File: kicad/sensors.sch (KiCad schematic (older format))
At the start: 4 parts

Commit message: snapshot
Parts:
- added I1, I2: INA381, HH_TexasInstruments:INA381-WSON, symbol HH_TexasInstruments:INA381
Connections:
- net GND: now also I1.4 (RESET), I1.PAD (GND), I2.4 (RESET), I2.PAD (GND)
- new net 3V3: I1.2 (VS+), I1.5 (CMPREF), I2.2 (VS+), I2.5 (CMPREF)
- new net OUT3: I1.6 (CMPIN), I1.7 (VOUT)
- new net OUT4: I2.6 (CMPIN), I2.7 (VOUT)
- new net S3+: I1.1 (IN+)
- new net S3-: I1.8 (IN-)
- new net S4+: I2.1 (IN+)
- new net S4-: I2.8 (IN-)
- no-connect marks 0 -> 2
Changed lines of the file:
@@
 Wire Wire Line
 	7150 4350 7150 4550
+$Comp
+L HH_TexasInstruments:INA381 I1
+U 1 1 5FC9F5FA
+P 5700 5400
+F 0 "I1" H 5700 5915 50  0000 C CNN
+F 1 "INA381" H 5700 5824 50  0000 C CNN
+F 2 "HH_TexasInstruments:INA381-WSON" H 5700 5400 50  0001 C CNN
+F 3 "https://www.ti.com/lit/ds/symlink/ina381.pdf" H 5700 5400 50  0001 C CNN
+F 4 "296-50475-1-ND" H 5700 5400 50  0001 C CNN "Digi-Key Part Number"
+F 5 "Texas Instruments" H 5700 5400 50  0001 C CNN "Manufacturer"
+F 6 "INA381A1IDSGR" H 5700 5400 50  0001 C CNN "Manufacturer Part Number"
+F 7 "LOW COST CURRENT SENSOR WITH COM" H 5700 5400 50  0001 C CNN "Description"
+	1    5700 5400
+	1    0    0    -1
+$EndComp
+$Comp
+L HH_TexasInstruments:INA381 I2
+U 1 1 5FC9FD95
+P 5700 6500
+F 0 "I2" H 5700 7015 50  0000 C CNN
+F 1 "INA381" H 5700 6924 50  0000 C CNN
+F 2 "HH_TexasInstruments:INA381-WSON" H 5700 6500 50  0001 C CNN
+F 3 "https://www.ti.com/lit/ds/symlink/ina381.pdf" H 5700 6500 50  0001 C CNN
+F 4 "296-50475-1-ND" H 5700 6500 50  0001 C CNN "Digi-Key Part Number"
+F 5 "Texas Instruments" H 5700 6500 50  0001 C CNN "Manufacturer"
+F 6 "INA381A1IDSGR" H 5700 6500 50  0001 C CNN "Manufacturer Part Number"
+F 7 "LOW COST CURRENT SENSOR WITH COM" H 5700 6500 50  0001 C CNN "Description"
+	1    5700 6500
+	1    0    0    -1
+$EndComp
+NoConn ~ 5100 5550
+NoConn ~ 5100 6650
+Text HLabel 7200 5950 2    50   Input ~ 0
+GND
+Wire Wire Line
+	6300 5250 6500 5250
+Wire Wire Line
+	7050 5250 7050 5950
+Wire Wire Line
+	7050 5950 7200 5950
+Wire Wire Line
+	7050 5950 7050 6350
+Wire Wire Line
+	7050 6350 6500 6350
+Connection ~ 7050 5950
+Wire Wire Line
+	6500 6350 6500 6450
+Wire Wire Line
+	6500 6450 6300 6450
+Connection ~ 6500 6350
+Wire Wire Line
+	6500 6350 6300 6350
+Wire Wire Line
+	6500 5250 6500 5350
+Wire Wire Line
+	6500 5350 6300 5350
+Connection ~ 6500 5250
+Wire Wire Line
+	6500 5250 7050 5250
+Text HLabel 7150 5150 2    50   Input ~ 0
+3V3
+Wire Wire Line
+	7150 5150 6700 5150
+Wire Wire Line
+	6700 5150 6700 6250
+Wire Wire Line
+	6700 6250 6300 6250
+Connection ~ 6700 5150
+Wire Wire Line
+	6700 5150 6300 5150
+Text HLabel 5100 5150 0    50   Input ~ 0
+S3+
+Text HLabel 5100 5250 0    50   Input ~ 0
+S3-
+Text HLabel 5100 6250 0    50   Input ~ 0
+S4+
+Text HLabel 5100 6350 0    50   Input ~ 0
+S4-
+Text HLabel 4600 5350 0    50   Input ~ 0
+OUT3
+Text HLabel 4600 6450 0    50   Input ~ 0
+OUT4
+Text HLabel 5100 5650 0    50   Input ~ 0
+3V3
+Text HLabel 5100 6750 0    50   Input ~ 0
+3V3
+Wire Wire Line
+	5100 5350 4800 5350
+Wire Wire Line
+	4800 5350 4800 5750
+Wire Wire Line
+	4800 5750 5100 5750
+Connection ~ 4800 5350
+Wire Wire Line
+	4800 5350 4600 5350
+Wire Wire Line
+	5100 6450 4800 6450
+Wire Wire Line
+	4800 6450 4800 6850
+Wire Wire Line
+	4800 6850 5100 6850
+Connection ~ 4800 6450
+Wire Wire Line
+	4800 6450 4600 6450
 $EndSCHEMATC

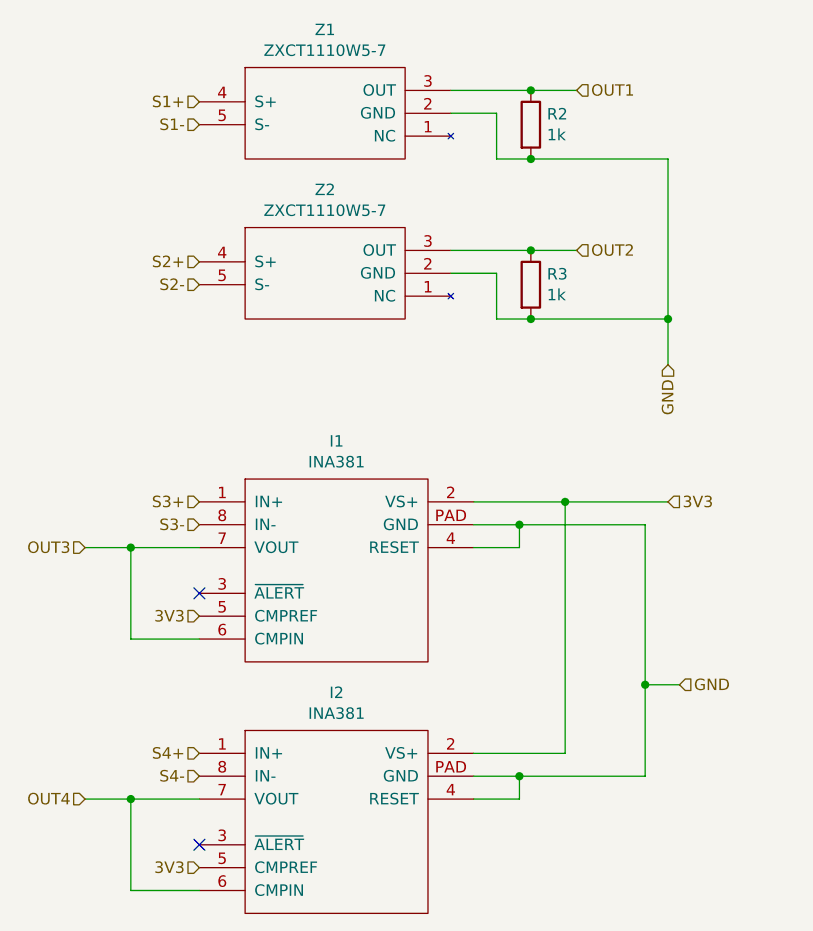
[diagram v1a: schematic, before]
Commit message: switch clock and add bypass
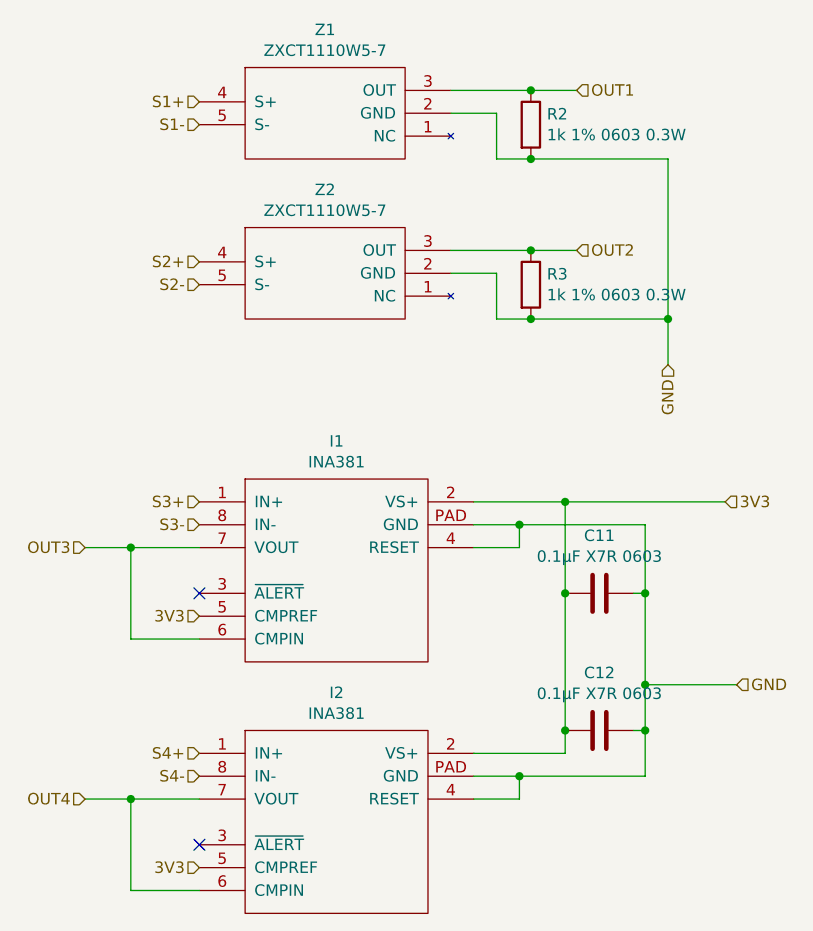
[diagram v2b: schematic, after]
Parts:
- added C11, C12: 0.1µF X7R 0603, Capacitor_SMD:C_0603_1608Metric, symbol Device:C
- R2, R3: value 1k -> 1k 1% 0603 0.3W
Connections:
- net 3V3: now also C11.2, C12.2
- net GND: now also C11.1, C12.1
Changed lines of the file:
@@
 P 6550 3500
 F 0 "R2" H 6620 3546 50  0000 L CNN
-F 1 "1k" H 6620 3455 50  0000 L CNN
+F 1 "1k 1% 0603 0.3W" H 6620 3455 50  0000 L CNN
 F 2 "Resistor_SMD:R_0603_1608Metric" V 6480 3500 50  0001 C CNN
 F 3 "~" H 6550 3500 50  0001 C CNN
@@
 P 6550 4200
 F 0 "R3" H 6620 4246 50  0000 L CNN
-F 1 "1k" H 6620 4155 50  0000 L CNN
+F 1 "1k 1% 0603 0.3W" H 6620 4155 50  0000 L CNN
 F 2 "Resistor_SMD:R_0603_1608Metric" V 6480 4200 50  0001 C CNN
 F 3 "~" H 6550 4200 50  0001 C CNN
@@
 NoConn ~ 5100 5550
 NoConn ~ 5100 6650
-Text HLabel 7200 5950 2    50   Input ~ 0
+Text HLabel 7450 5950 2    50   Input ~ 0
 GND
 Wire Wire Line
 	6300 5250 6500 5250
 Wire Wire Line
-	7050 5250 7050 5950
+	7050 5250 7050 5550
 Wire Wire Line
-	7050 5950 7200 5950
-Wire Wire Line
-	7050 5950 7050 6350
+	7050 5950 7050 6150
 Wire Wire Line
 	7050 6350 6500 6350
@@
 Wire Wire Line
 	6500 5250 7050 5250
-Text HLabel 7150 5150 2    50   Input ~ 0
+Text HLabel 7400 5150 2    50   Input ~ 0
 3V3
 Wire Wire Line
-	7150 5150 6700 5150
-Wire Wire Line
-	6700 5150 6700 6250
+	6700 5150 6700 5550
 Wire Wire Line
 	6700 6250 6300 6250
@@
 Wire Wire Line
 	4800 6450 4600 6450
+$Comp
+L Device:C C11
+U 1 1 5FCEF4F8
+P 6850 5550
+F 0 "C11" V 6598 5550 50  0000 C CNN
+F 1 "0.1µF X7R 0603" V 6689 5550 50  0000 C CNN
+F 2 "Capacitor_SMD:C_0603_1608Metric" H 6888 5400 50  0001 C CNN
+F 3 "~" H 6850 5550 50  0001 C CNN
+	1    6850 5550
+	0    1    1    0
+$EndComp
+Connection ~ 6700 5550
+Wire Wire Line
+	6700 5550 6700 6150
+$Comp
+L Device:C C12
+U 1 1 5FCF3DBC
+P 6850 6150
+F 0 "C12" V 6598 6150 50  0000 C CNN
+F 1 "0.1µF X7R 0603" V 6689 6150 50  0000 C CNN
+F 2 "Capacitor_SMD:C_0603_1608Metric" H 6888 6000 50  0001 C CNN
+F 3 "~" H 6850 6150 50  0001 C CNN
+	1    6850 6150
+	0    1    1    0
+$EndComp
+Connection ~ 6700 6150
+Wire Wire Line
+	6700 6150 6700 6250
+Wire Wire Line
+	6700 5150 7400 5150
+Wire Wire Line
+	7050 5950 7450 5950
+Wire Wire Line
+	7000 5550 7050 5550
+Connection ~ 7050 5550
+Wire Wire Line
+	7050 5550 7050 5950
+Wire Wire Line
+	7000 6150 7050 6150
+Connection ~ 7050 6150
+Wire Wire Line
+	7050 6150 7050 6350
 $EndSCHEMATC
